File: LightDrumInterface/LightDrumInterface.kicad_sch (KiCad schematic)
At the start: 53 parts, among them J1 MIDI-IN, J2 DEBUG-CONN, J3 MIDI-OUT, J4 PWR-CONN, J5 0525593652, J6 0541323662, SW1 RESET-SW, U1 STP16CP05, U2 TPL0401B-10-Q1, U3 74AUP2G04, U4 PC817

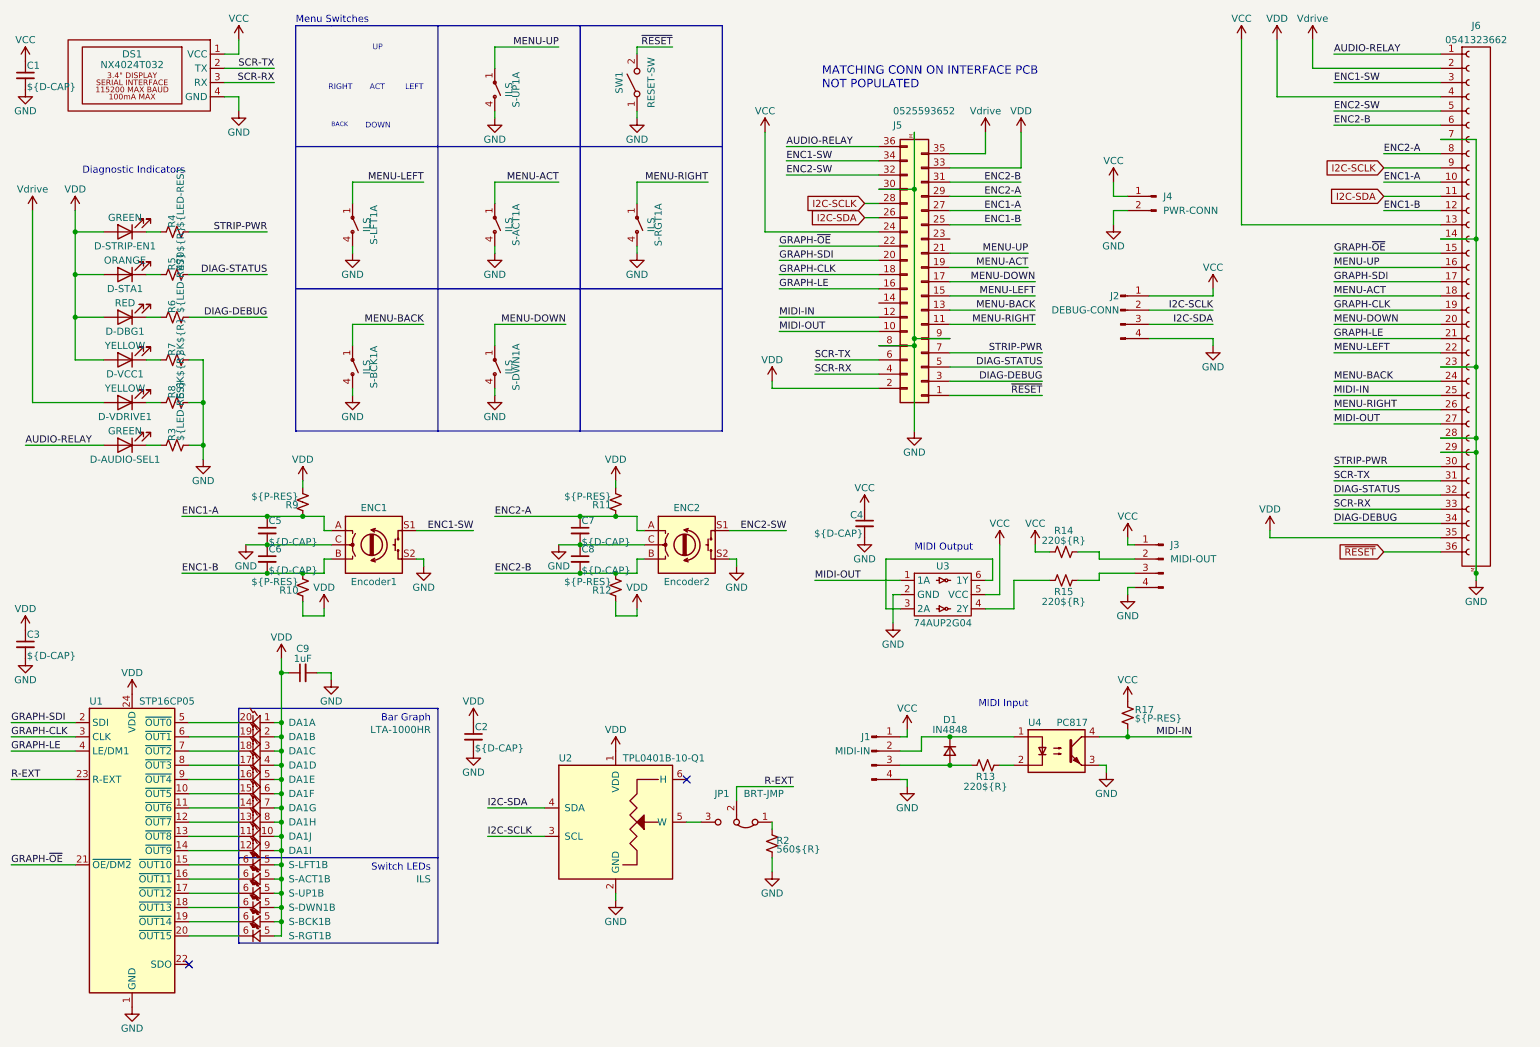
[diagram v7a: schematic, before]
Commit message: Replace barrel jacks with proper DIN4 conn and more
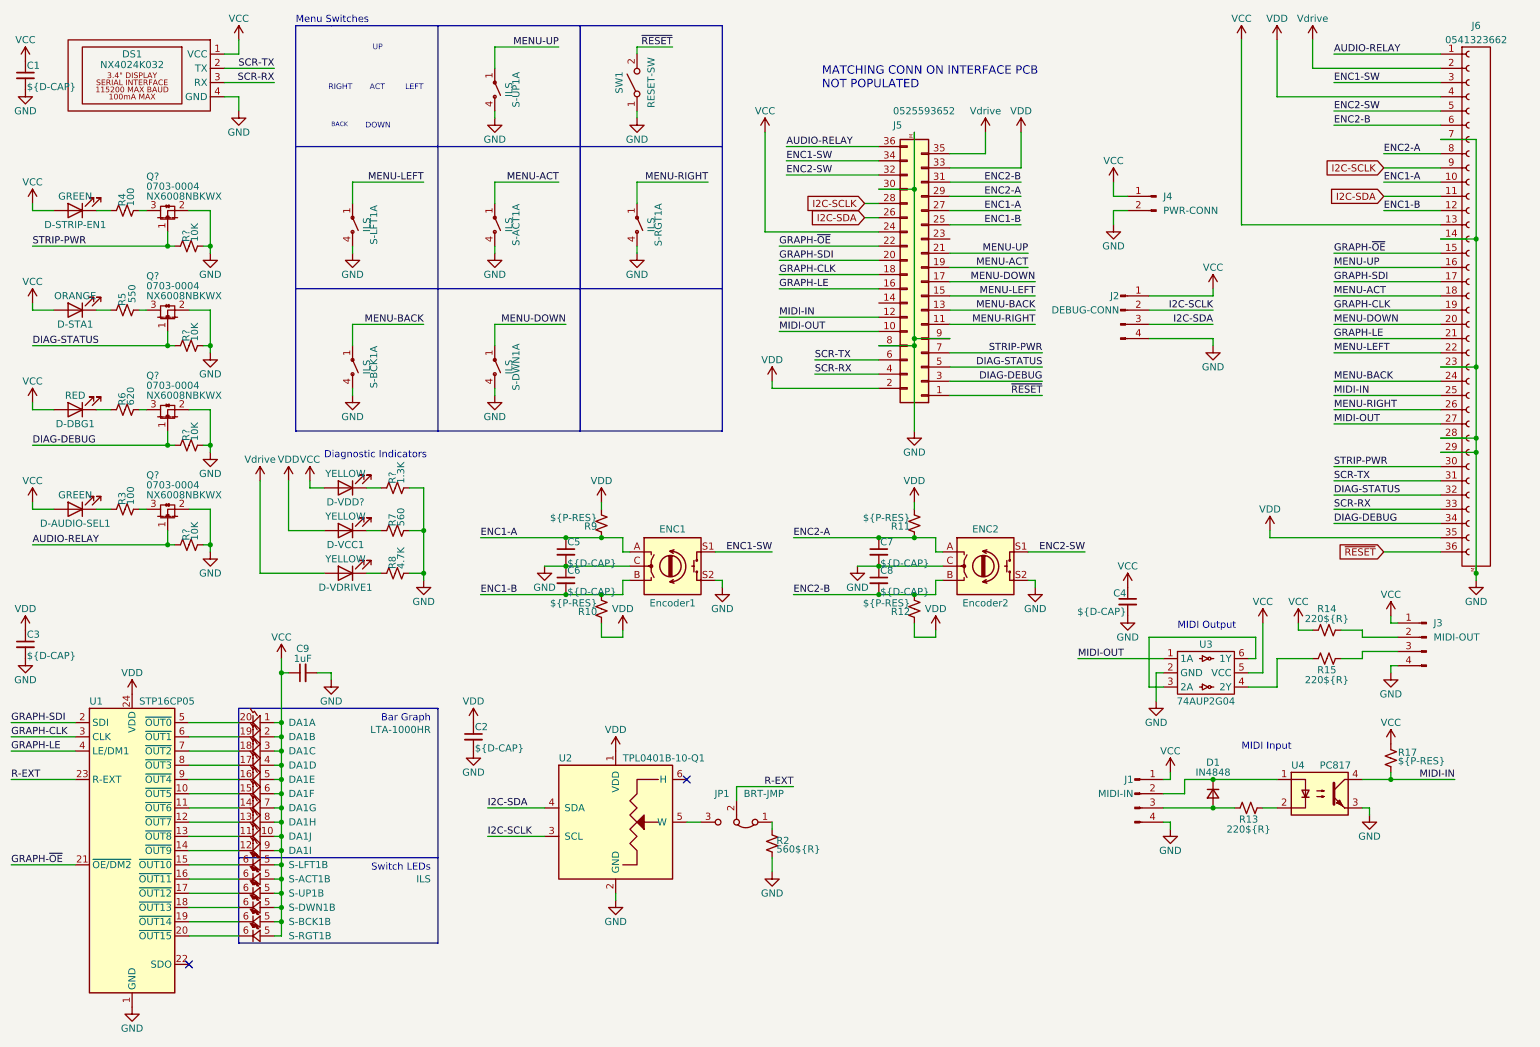
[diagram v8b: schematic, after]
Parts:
- added D-VDD?: YELLOW, LED_SMD:LED_0805_2012Metric, symbol Device:LED
- added Q? (x4): NX6008NBKWX, Package_TO_SOT_SMD:SOT-323_SC-70, symbol Daxxn_Transistors:NX6008NBKWX
- added R? (x4): 10K, Resistor_SMD:R_0805_2012Metric, symbol Device:R_Small_US
- added R?: 1.3K, Resistor_SMD:R_0805_2012Metric, symbol Device:R_Small_US
- DS1: value NX4024T032 -> NX4024K032
- R3, R4: value ${LED-RES} -> 100
- R5: value 470${R} -> 550
- R6: value ${LED-RES} -> 620
- R7: value 3K${R} -> 560
- R8: value 5.6K${R} -> 4.7K
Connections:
- net AUDIO-RELAY: now also Q?.1 (G), R?.1; no longer D-AUDIO-SEL1.2 (A)
- net DIAG-DEBUG: now also Q?.1 (G), R?.1; no longer R6.2
- net DIAG-STATUS: now also Q?.1 (G), R?.1; no longer R5.2
- net GND: now also Q?.2 (S), Q?.2 (S), Q?.2 (S), Q?.2 (S), R?.2, R?.2, R?.2, R?.2, R?.2; no longer R3.2
- net STRIP-PWR: now also Q?.1 (G), R?.1; no longer R4.2
- net VCC: now also C9.1, D-AUDIO-SEL1.2 (A), D-DBG1.2 (A), D-STA1.2 (A), D-STRIP-EN1.2 (A), DA1.1, DA1.10, DA1.2, DA1.3, DA1.4, DA1.5, DA1.6, DA1.7, DA1.8, DA1.9, S-ACT1.5, S-BCK1.5, S-DWN1.5, S-LFT1.5, S-RGT1.5, S-UP1.5, D-VDD?.2 (A)
- net VDD: no longer C9.1, D-DBG1.2 (A), D-STA1.2 (A), D-STRIP-EN1.2 (A), DA1.1, DA1.10, DA1.2, DA1.3, DA1.4, DA1.5, DA1.6, DA1.7, DA1.8, DA1.9, S-ACT1.5, S-BCK1.5, S-DWN1.5, S-LFT1.5, S-RGT1.5, S-UP1.5
- new net: Q?.3 (D), R3.2
- new net: Q?.3 (D), R5.2
- new net: Q?.3 (D), R6.2
- new net: Q?.3 (D), R4.2
- new net: D-VDD?.1 (K), R?.1
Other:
- moved on the sheet: C4, C5, C6, C7, C8, D-AUDIO-SEL1, D-DBG1, D-STA1, D-STRIP-EN1, D-VCC1, D-VDRIVE1, D1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
